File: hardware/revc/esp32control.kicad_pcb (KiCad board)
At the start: 2 copper layers, 67.6 x 85.9 mm, 96 parts, among them J1 Conn_02x10_Odd_Even, Q101 2N7002, Q102 2N7002, Q202 DMP4015SK3, Q302 DMP4015SK3, Q402 DMP4015SK3, Q502 DMP4015SK3, Q7 MMBT3904, Q8 MMBT3904, SW1 Boot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

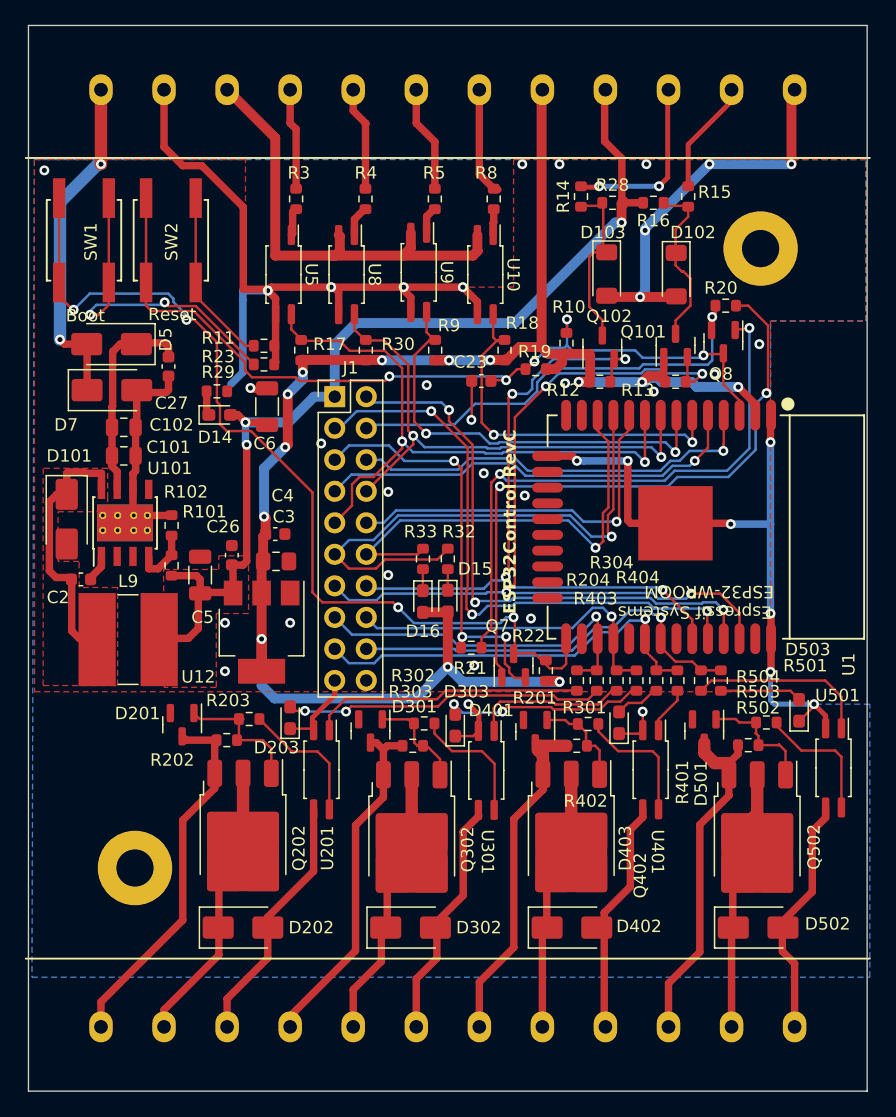
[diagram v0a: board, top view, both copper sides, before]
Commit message: workflow fix (#2)
* remove inner layer in yaml

* fixed erc

* fixed drc

* updated wroom32 fp

* updated kibot

* updated pcb

* updated pcb

* updated yml

* yml updates

* fixed layer entries

* updated sch, pcb, bom

* reduced drc verbosity
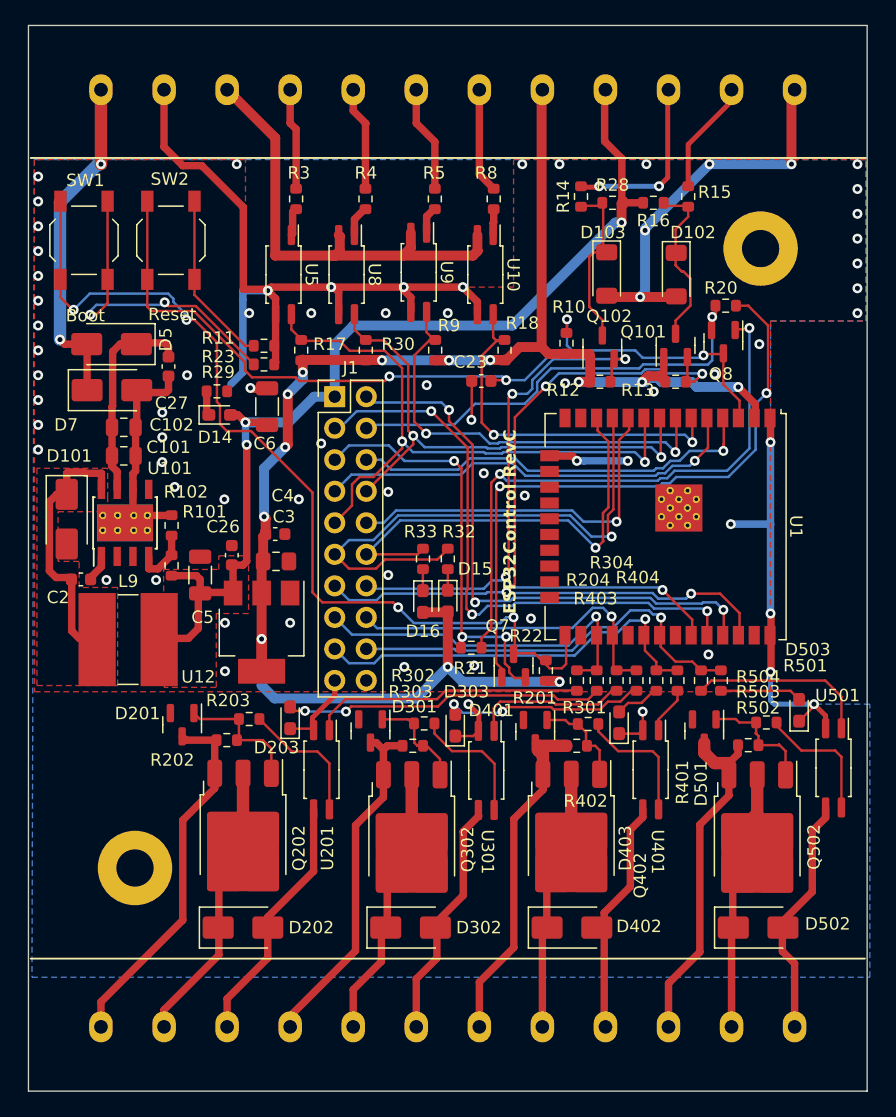
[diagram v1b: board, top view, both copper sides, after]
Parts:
- removed R19: nb, Resistor_SMD:R_0603_1608Metric
- C23: value 100n 50V -> 1u 25V
- D201, D301, D401, D501: value BZX84Cxx -> BZX84C10
- Q202, Q302, Q402, Q502: value DMP4015SK3 -> HSU4113
- R101: value 10k -> 12k
- R102: value 3k24 -> 3k9
- SW1, SW2: footprint switches:SMD_Switch_6.5x6 -> Button_Switch_SMD:SW_SPST_TL3342
- U1: footprint ESP32-footprints-Lib:ESP32-WROOM -> RF_Module:ESP32-WROOM-32UE
- moved U1 3.25 mm to (102.9, 76.6), turned to -90 degrees
- turned SW1 to -90 degrees
- turned SW2 to -90 degrees
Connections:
- net /OPTO3 renamed /IO35
- net /OPTO4 renamed /IO34
- net /dig_output/Out renamed /OUT1
- U1 pad 26: /IO4 -> unconnected-(U1-IO4-Pad26)
- U1 pad 37: /IO23 -> unconnected-(U1-IO23-Pad37)
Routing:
- net GND: track 184.7 -> 171.1 mm, vias 38 -> 72
- net +3V3: track 137.9 -> 135.5 mm
- net Net-(R15-Pad2): track 9.34 -> 8.29 mm
- net Net-(R11-Pad1): track 13.2 -> 14.1 mm
- net /sheet5C1F370F/Vin: track 28.4 -> 27.5 mm
- net /nBoot: track 74.2 -> 75.0 mm
- net Net-(D201-A): track 11.0 -> 10.4 mm
- net /nReset: track 69.7 -> 69.8 mm, vias 5 -> 4
